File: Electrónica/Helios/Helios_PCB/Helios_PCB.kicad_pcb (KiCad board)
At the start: 2 copper layers, 6 parts, among them U0 OPA2380, U1 OPA2380

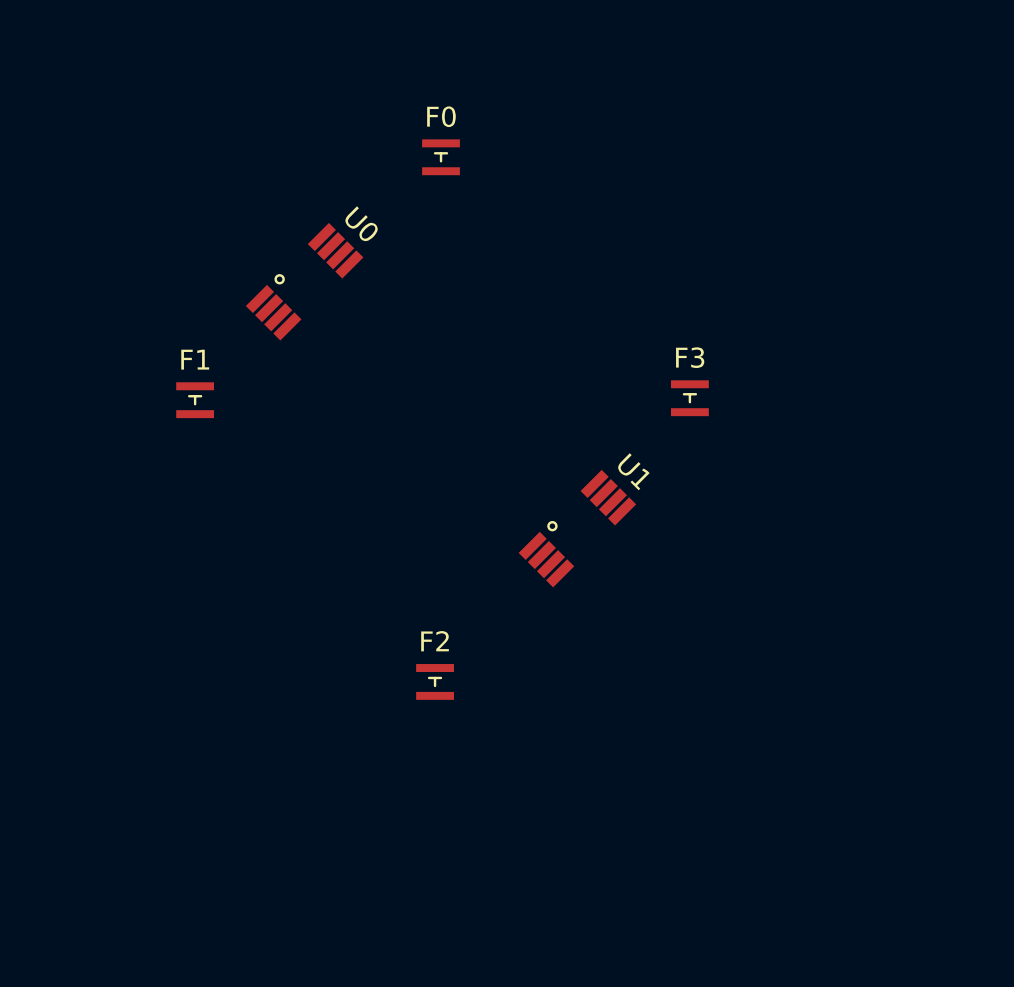
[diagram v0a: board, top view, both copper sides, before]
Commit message: Helios -  Added Connectors
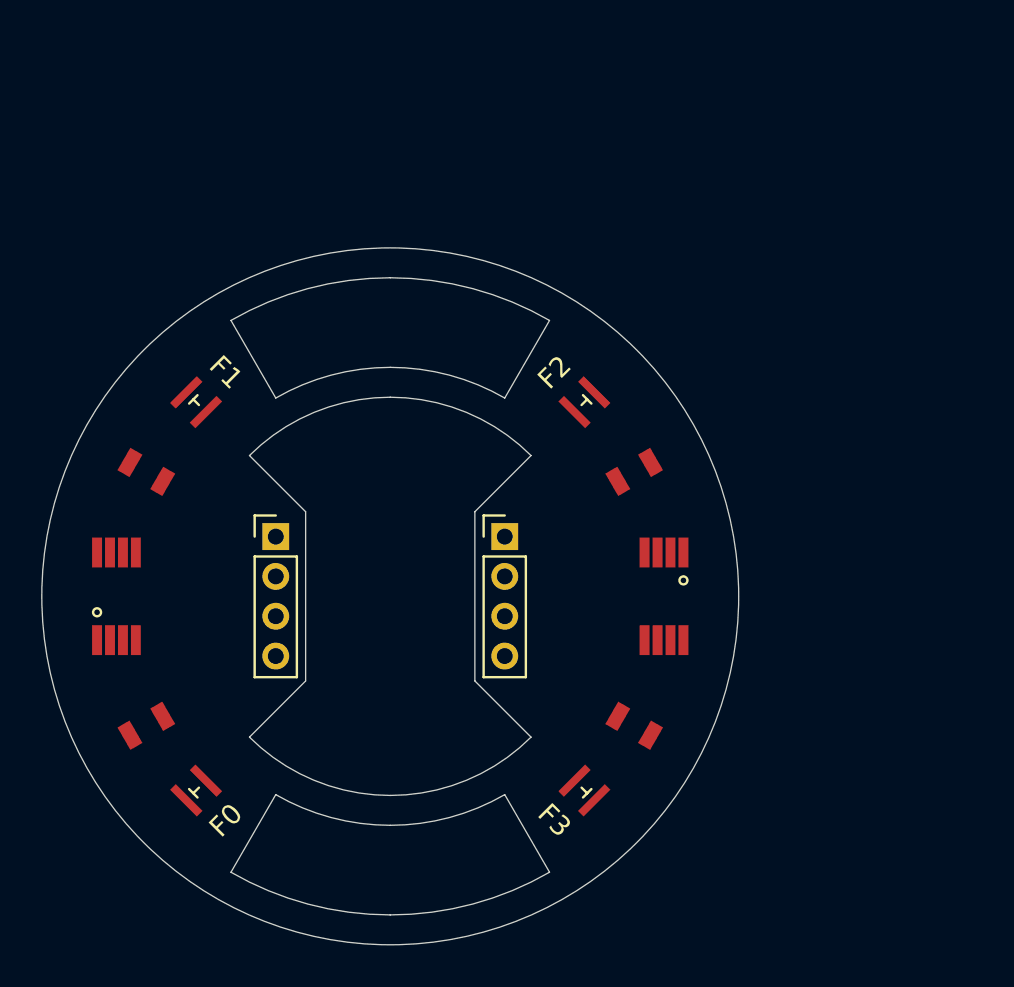
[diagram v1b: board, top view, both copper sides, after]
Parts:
- added J0: Connector J0, Connector_PinHeader_2.00mm:PinHeader_1x04_P2.00mm_Vertical, F.Cu at (144.2, 97.0)
- added J1: Connector J1, Connector_PinHeader_2.00mm:PinHeader_1x04_P2.00mm_Vertical, F.Cu at (155.8, 97.0)
- added R0: R, Helios:RS_0805, F.Cu at (137.8, 106.5)
- added R1: R, Helios:RS_0805, F.Cu at (137.8, 93.8)
- added R2: R, Helios:RS_0805, F.Cu at (162.2, 93.8)
- added R3: R, Helios:RS_0805, F.Cu at (162.2, 106.5)
- moved F0 34.1 mm to (140.2, 109.8), turned to 135 degrees
- moved F3 20.4 mm to (159.8, 109.8), turned to 225 degrees
- moved U0 18.4 mm to (136.2, 100.0), turned to 0 degrees
- moved F2 15.9 mm to (159.8, 90.2), turned to 315 degrees
- moved U1 5.52 mm to (163.8, 100.0), turned to 180 degrees
- moved F1 0.11 mm to (140.2, 90.2), turned to 45 degrees
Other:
- board outline added: 35 x 35 mm

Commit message: Helios: VCC routing
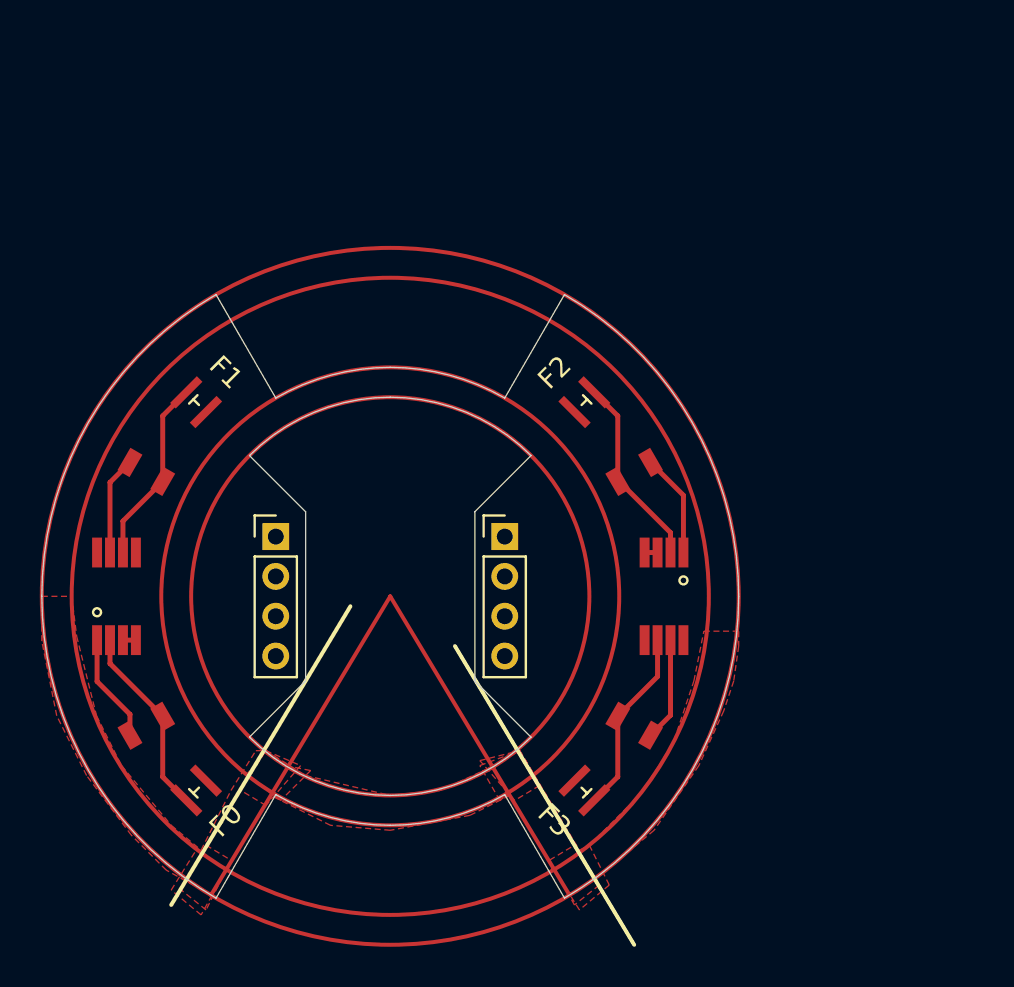
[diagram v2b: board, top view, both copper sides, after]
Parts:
- turned R2 to -150 degrees
- turned R3 to 150 degrees
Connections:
- R0 pad 1: O0 -> O1
- R1 pad 1: O1 -> O0
- U0 pad 1: O0 -> O1
- U0 pad 7: O1 -> O0
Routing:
- net Net-(F2-Pad1): track 0.00 -> 9.67 mm
- net Net-(F0-Pad1): track 0.00 -> 9.64 mm
- net Net-(F3-Pad1): track 0.00 -> 9.36 mm
- net Net-(F1-Pad1): track 0.00 -> 9.36 mm
- net O1: track 0.00 -> 5.49 mm
- net O2: track 0.00 -> 5.21 mm
- net O3: track 0.00 -> 5.19 mm
- net O0: track 0.00 -> 4.94 mm
- net GND: track 0.00 -> 1.30 mm
- added copper zone on F.Cu, net VCC
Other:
- board size 35 x 35 mm -> 35 x 30.3 mm
- net class Default removed

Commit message: Helios: Top Layer
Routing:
- net GND: track 1.30 -> 60.4 mm
- net O2: track 5.21 -> 16.5 mm
- net O1: track 5.49 -> 16.4 mm
- net O0: track 4.94 -> 15.6 mm
- net O3: track 5.19 -> 15.4 mm
- net VCC: track 0.00 -> 7.61 mm
- added copper zone on F.Cu, net GND
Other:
- outline, holes or cut-outs redrawn

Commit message: Revert "Revert "Helios: Bot Layer Sch. (LEDs)""
This reverts commit 5c5999d2bbe18ce28315539fce76e1635c27d7e8.
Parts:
- added D0: LED, LED_SMD:LED_PLCC-2, B.Cu at (170.9, 78.2)
- added D1: LED, LED_SMD:LED_PLCC-2, B.Cu at (140.2, 90.2)
- added D2: LED, LED_SMD:LED_PLCC-2, B.Cu at (177.1, 78.2)
- added D3: LED, LED_SMD:LED_PLCC-2, B.Cu at (170.9, 73.5)
- added Q1: AO3400A, Package_TO_SOT_SMD:SOT-23, B.Cu at (165.4, 73.3)
- added R5: R, Helios:RS_0805, B.Cu at (166.0, 76.7)

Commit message: Revert "Helios: Bot Layer Sch. (LEDs)"
This reverts commit dca8e3bb9b15b9e1c7b2acfc811398ae5ce91dcf.
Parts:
- removed D0, D1, D2, D3: LED, LED_SMD:LED_PLCC-2
- removed Q1: AO3400A, Package_TO_SOT_SMD:SOT-23
- removed R5: R, Helios:RS_0805
